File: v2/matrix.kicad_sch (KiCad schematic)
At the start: 136 parts, among them SW10 SW_Push, SW11 SW_Push, SW12 SW_Push, SW13 SW_Push, SW14 SW_Push, SW15 SW_Push, SW16 SW_Push, SW17 SW_Push, SW18 SW_Push, SW19 SW_Push, SW20 SW_Push, SW21 SW_Push, SW22 SW_Push, SW23 SW_Push, SW24 SW_Push, SW25 SW_Push, SW26 SW_Push, SW27 SW_Push, SW28 SW_Push, SW29 SW_Push, SW3 SW_Push, SW30 SW_Push, SW31 SW_Push, SW32 SW_Push, SW33 SW_Push, SW34 SW_Push, SW35 SW_Push, SW36 SW_Push, SW37 SW_Push, SW38 SW_Push, SW39 SW_Push, SW4 SW_Push, SW40 SW_Push, SW41 SW_Push, SW42 SW_Push, SW43 SW_Push, SW44 SW_Push, SW45 SW_Push, SW46 SW_Push, SW47 SW_Push, SW48 SW_Push, SW49 SW_Push, SW5 SW_Push, SW50 SW_Push, SW51 SW_Push, SW52 SW_Push, SW53 SW_Push, SW54 SW_Push, SW55 SW_Push, SW56 SW_Push, SW57 SW_Push, SW58 SW_Push, SW59 SW_Push, SW6 SW_Push, SW60 SW_Push, SW61 SW_Push, SW62 SW_Push, SW63 SW_Push, SW64 SW_Push, SW65 SW_Push, SW66 SW_Push, SW67 SW_Push, SW68 SW_Push, SW69 SW_Push, SW7 SW_Push, SW70 SW_Push, SW8 SW_Push, SW9 SW_Push

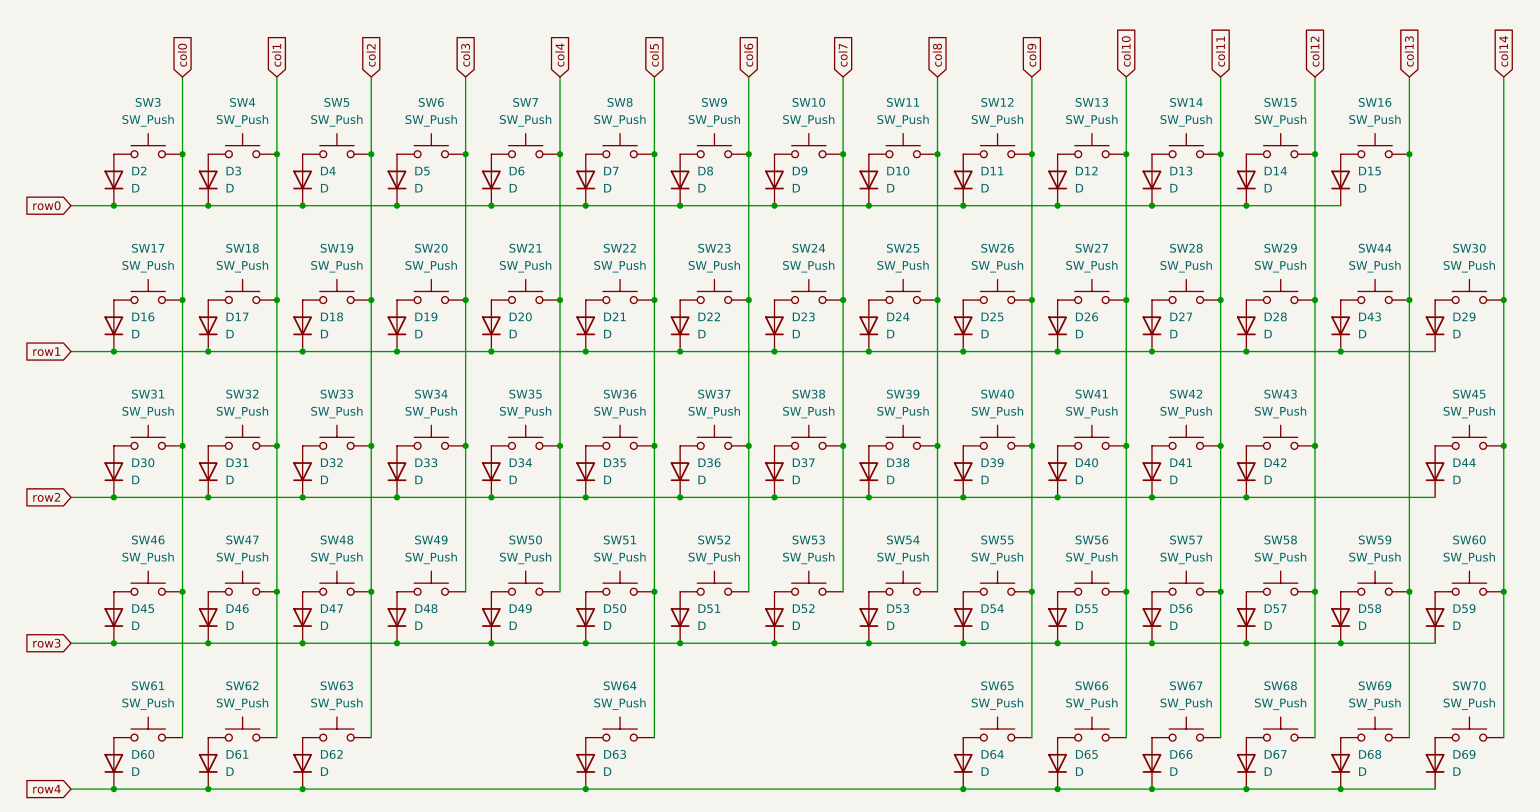
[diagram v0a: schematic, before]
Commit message: Changed switch value for better understanding in PCB view
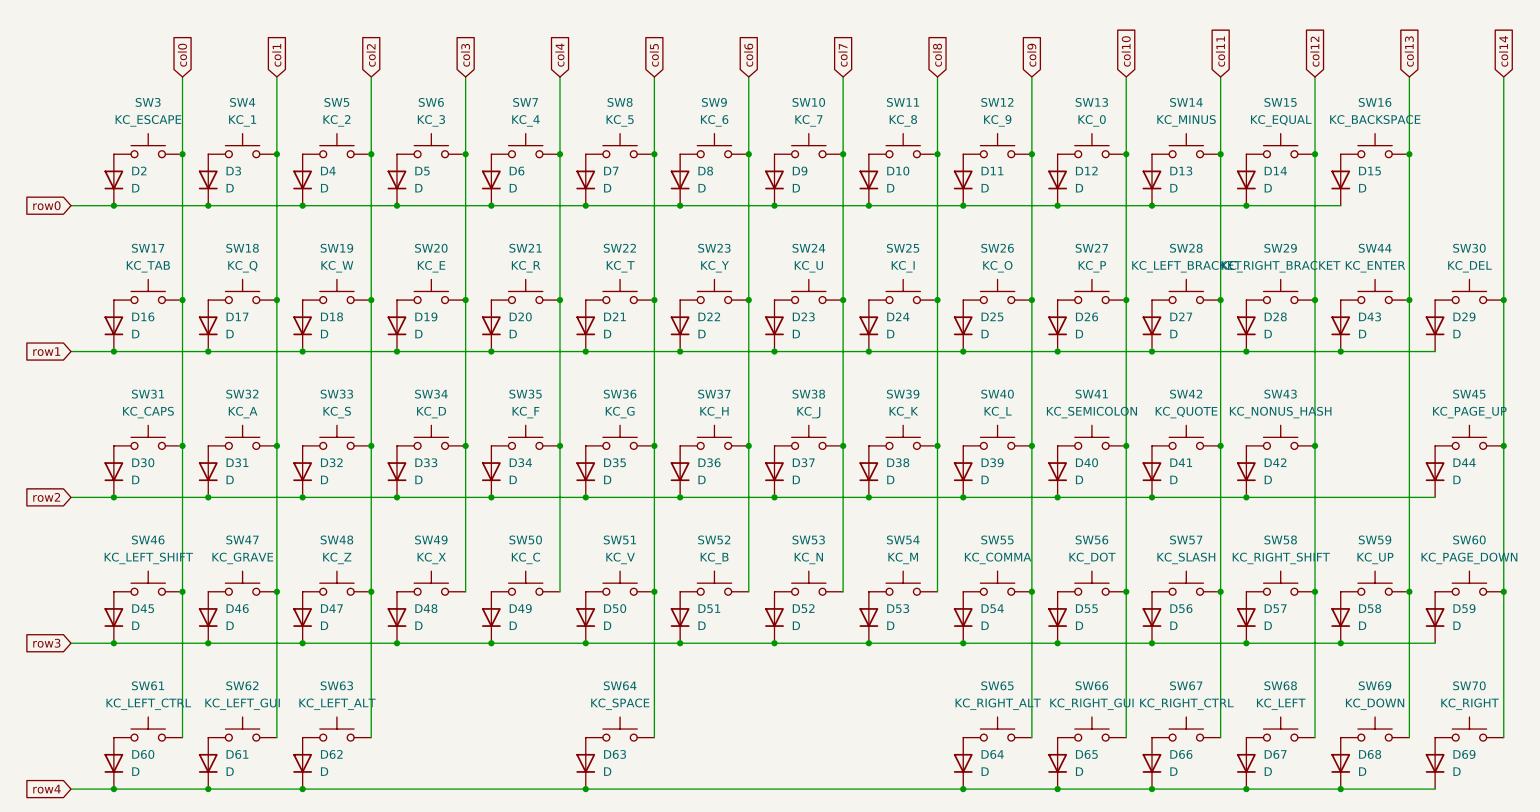
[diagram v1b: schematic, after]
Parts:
- SW10: value SW_Push -> KC_7
- SW11: value SW_Push -> KC_8
- SW12: value SW_Push -> KC_9
- SW13: value SW_Push -> KC_0
- SW14: value SW_Push -> KC_MINUS
- SW15: value SW_Push -> KC_EQUAL
- SW16: value SW_Push -> KC_BACKSPACE
- SW17: value SW_Push -> KC_TAB
- SW18: value SW_Push -> KC_Q
- SW19: value SW_Push -> KC_W
- SW20: value SW_Push -> KC_E
- SW21: value SW_Push -> KC_R
- SW22: value SW_Push -> KC_T
- SW23: value SW_Push -> KC_Y
- SW24: value SW_Push -> KC_U
- SW25: value SW_Push -> KC_I
- SW26: value SW_Push -> KC_O
- SW27: value SW_Push -> KC_P
- SW28: value SW_Push -> KC_LEFT_BRACKET
- SW29: value SW_Push -> KC_RIGHT_BRACKET
- SW3: value SW_Push -> KC_ESCAPE
- SW30: value SW_Push -> KC_DEL
- SW31: value SW_Push -> KC_CAPS
- SW32: value SW_Push -> KC_A
- SW33: value SW_Push -> KC_S
- SW34: value SW_Push -> KC_D
- SW35: value SW_Push -> KC_F
- SW36: value SW_Push -> KC_G
- SW37: value SW_Push -> KC_H
- SW38: value SW_Push -> KC_J
- SW39: value SW_Push -> KC_K
- SW4: value SW_Push -> KC_1
- SW40: value SW_Push -> KC_L
- SW41: value SW_Push -> KC_SEMICOLON
- SW42: value SW_Push -> KC_QUOTE
- SW43: value SW_Push -> KC_NONUS_HASH
- SW44: value SW_Push -> KC_ENTER
- SW45: value SW_Push -> KC_PAGE_UP
- SW46: value SW_Push -> KC_LEFT_SHIFT
- SW47: value SW_Push -> KC_GRAVE
- SW48: value SW_Push -> KC_Z
- SW49: value SW_Push -> KC_X
- SW5: value SW_Push -> KC_2
- SW50: value SW_Push -> KC_C
- SW51: value SW_Push -> KC_V
- SW52: value SW_Push -> KC_B
- SW53: value SW_Push -> KC_N
- SW54: value SW_Push -> KC_M
- SW55: value SW_Push -> KC_COMMA
- SW56: value SW_Push -> KC_DOT
- SW57: value SW_Push -> KC_SLASH
- SW58: value SW_Push -> KC_RIGHT_SHIFT
- SW59: value SW_Push -> KC_UP
- SW6: value SW_Push -> KC_3
- SW60: value SW_Push -> KC_PAGE_DOWN
- SW61: value SW_Push -> KC_LEFT_CTRL
- SW62: value SW_Push -> KC_LEFT_GUI
- SW63: value SW_Push -> KC_LEFT_ALT
- SW64: value SW_Push -> KC_SPACE
- SW65: value SW_Push -> KC_RIGHT_ALT
- SW66: value SW_Push -> KC_RIGHT_GUI
- SW67: value SW_Push -> KC_RIGHT_CTRL
- SW68: value SW_Push -> KC_LEFT
- SW69: value SW_Push -> KC_DOWN
- SW7: value SW_Push -> KC_4
- SW70: value SW_Push -> KC_RIGHT
- SW8: value SW_Push -> KC_5
- SW9: value SW_Push -> KC_6
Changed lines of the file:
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@@
 			)
 		)
-		(property "Value" "SW_Push"
+		(property "Value" "KC_E"
 			(at 121.92 76.2 0)
 			(effects
@@
 			)
 		)
-		(property "Value" "SW_Push"
+		(property "Value" "KC_Q"
 			(at 93.98 76.2 0)
 			(effects
@@
 			)
 		)
-		(property "Value" "SW_Push"
+		(property "Value" "KC_SPACE"
 			(at 149.86 140.97 0)
 			(effects
@@
 			)
 		)
-		(property "Value" "SW_Push"
+		(property "Value" "KC_EQUAL"
 			(at 247.65 54.61 0)
 			(effects
@@
 			)
 		)
-		(property "Value" "SW_Push"
+		(property "Value" "KC_8"
 			(at 191.77 54.61 0)
 			(effects
@@
 			)
 		)
-		(property "Value" "SW_Push"
+		(property "Value" "KC_B"
 			(at 163.83 119.38 0)
 			(effects
@@
 			)
 		)
-		(property "Value" "SW_Push"
+		(property "Value" "KC_T"
 			(at 149.86 76.2 0)
 			(effects
@@
 			)
 		)
-		(property "Value" "SW_Push"
+		(property "Value" "KC_LEFT_ALT"
 			(at 107.95 140.97 0)
 			(effects
@@
 			)
 		)
-		(property "Value" "SW_Push"
+		(property "Value" "KC_RIGHT"
 			(at 275.59 140.97 0)
 			(effects
@@
 			)
 		)
-		(property "Value" "SW_Push"
+		(property "Value" "KC_RIGHT_GUI"
 			(at 219.71 140.97 0)
 			(effects
@@
 			)
 		)
-		(property "Value" "SW_Push"
+		(property "Value" "KC_LEFT_BRACKET"
 			(at 233.68 76.2 0)
 			(effects
@@
 			)
 		)
-		(property "Value" "SW_Push"
+		(property "Value" "KC_LEFT_CTRL"
 			(at 80.01 140.97 0)
 			(effects
@@
 			)
 		)
-		(property "Value" "SW_Push"
+		(property "Value" "KC_4"
 			(at 135.89 54.61 0)
 			(effects
@@
 			)
 		)
-		(property "Value" "SW_Push"
+		(property "Value" "KC_K"
 			(at 191.77 97.79 0)
 			(effects
@@
 			)
 		)
-		(property "Value" "SW_Push"
+		(property "Value" "KC_L"
 			(at 205.74 97.79 0)
 			(effects
@@
 			)
 		)
-		(property "Value" "SW_Push"
+		(property "Value" "KC_LEFT_GUI"
 			(at 93.98 140.97 0)
 			(effects
@@
 			)
 		)
-		(property "Value" "SW_Push"
+		(property "Value" "KC_RIGHT_SHIFT"
 			(at 247.65 119.38 0)
 			(effects
@@
 			)
 		)
-		(property "Value" "SW_Push"
+		(property "Value" "KC_H"
 			(at 163.83 97.79 0)
 			(effects
@@
 			)
 		)
-		(property "Value" "SW_Push"
+		(property "Value" "KC_Y"
 			(at 163.83 76.2 0)
 			(effects
@@
 			)
 		)
-		(property "Value" "SW_Push"
+		(property "Value" "KC_GRAVE"
 			(at 93.98 119.38 0)
 			(effects
@@
 			)
 		)
-		(property "Value" "SW_Push"
+		(property "Value" "KC_NONUS_HASH"
 			(at 247.65 97.79 0)
 			(effects
@@
 			)
 		)
-		(property "Value" "SW_Push"
+		(property "Value" "KC_O"
 			(at 205.74 76.2 0)
 			(effects
@@
 			)
 		)
-		(property "Value" "SW_Push"
+		(property "Value" "KC_QUOTE"
 			(at 233.68 97.79 0)
 			(effects
@@
 			)
 		)
-		(property "Value" "SW_Push"
+		(property "Value" "KC_1"
 			(at 93.98 54.61 0)
 			(effects
@@
 			)
 		)
-		(property "Value" "SW_Push"
+		(property "Value" "KC_COMMA"
 			(at 205.74 119.38 0)
 			(effects
@@
 			)
 		)
-		(property "Value" "SW_Push"
+		(property "Value" "KC_TAB"
 			(at 80.01 76.2 0)
 			(effects
@@
 			)
 		)
-		(property "Value" "SW_Push"
+		(property "Value" "KC_BACKSPACE"
 			(at 261.62 54.61 0)
 			(effects
@@
 			)
 		)
-		(property "Value" "SW_Push"
+		(property "Value" "KC_LEFT"
 			(at 247.65 140.97 0)
 			(effects
@@
 			)
 		)
-		(property "Value" "SW_Push"
+		(property "Value" "KC_C"
 			(at 135.89 119.38 0)
 			(effects
@@
 			)
 		)
-		(property "Value" "SW_Push"
+		(property "Value" "KC_9"
 			(at 205.74 54.61 0)
 			(effects
@@
 			)
 		)
-		(property "Value" "SW_Push"
+		(property "Value" "KC_3"
 			(at 121.92 54.61 0)
 			(effects
@@
 			)
 		)
-		(property "Value" "SW_Push"
+		(property "Value" "KC_SEMICOLON"
 			(at 219.71 97.79 0)
 			(effects
@@
 			)
 		)
-		(property "Value" "SW_Push"
+		(property "Value" "KC_DEL"
 			(at 275.59 76.2 0)
 			(effects
@@
 			)
 		)
-		(property "Value" "SW_Push"
+		(property "Value" "KC_SLASH"
 			(at 233.68 119.38 0)
 			(effects
@@
 			)
 		)
-		(property "Value" "SW_Push"
+		(property "Value" "KC_RIGHT_ALT"
 			(at 205.74 140.97 0)
 			(effects
@@
 			)
 		)
-		(property "Value" "SW_Push"
+		(property "Value" "KC_G"
 			(at 149.86 97.79 0)
 			(effects
@@
 			)
 		)
-		(property "Value" "SW_Push"
+		(property "Value" "KC_DOWN"
 			(at 261.62 140.97 0)
 			(effects
@@
 			)
 		)
-		(property "Value" "SW_Push"
+		(property "Value" "KC_P"
 			(at 219.71 76.2 0)
 			(effects
@@
 			)
 		)
-		(property "Value" "SW_Push"
+		(property "Value" "KC_A"
 			(at 93.98 97.79 0)
 			(effects
@@
 			)
 		)
-		(property "Value" "SW_Push"
+		(property "Value" "KC_W"
 			(at 107.95 76.2 0)
 			(effects
@@
 			)
 		)
-		(property "Value" "SW_Push"
+		(property "Value" "KC_S"
 			(at 107.95 97.79 0)
 			(effects
@@
 			)
 		)
-		(property "Value" "SW_Push"
+		(property "Value" "KC_ESCAPE"
 			(at 80.01 54.61 0)
 			(effects
@@
 			)
 		)
-		(property "Value" "SW_Push"
+		(property "Value" "KC_RIGHT_BRACKET"
 			(at 247.65 76.2 0)
 			(effects
@@
 			)
 		)
-		(property "Value" "SW_Push"
+		(property "Value" "KC_I"
 			(at 191.77 76.2 0)
 			(effects
@@
 			)
 		)
-		(property "Value" "SW_Push"
+		(property "Value" "KC_RIGHT_CTRL"
 			(at 233.68 140.97 0)
 			(effects
@@
 			)
 		)
-		(property "Value" "SW_Push"
+		(property "Value" "KC_U"
 			(at 177.8 76.2 0)
 			(effects
@@
 			)
 		)
-		(property "Value" "SW_Push"
+		(property "Value" "KC_6"
 			(at 163.83 54.61 0)
 			(effects
@@
 			)
 		)
-		(property "Value" "SW_Push"
+		(property "Value" "KC_PAGE_UP"
 			(at 275.59 97.79 0)
 			(effects
@@
 			)
 		)
-		(property "Value" "SW_Push"
+		(property "Value" "KC_5"
 			(at 149.86 54.61 0)
 			(effects
@@
 			)
 		)
-		(property "Value" "SW_Push"
+		(property "Value" "KC_2"
 			(at 107.95 54.61 0)
 			(effects
@@
 			)
 		)
-		(property "Value" "SW_Push"
+		(property "Value" "KC_Z"
 			(at 107.95 119.38 0)
 			(effects
@@
 			)
 		)
-		(property "Value" "SW_Push"
+		(property "Value" "KC_ENTER"
 			(at 261.62 76.2 0)
 			(effects
@@
 			)
 		)
-		(property "Value" "SW_Push"
+		(property "Value" "KC_DOT"
 			(at 219.71 119.38 0)
 			(effects
@@
 			)
 		)
-		(property "Value" "SW_Push"
+		(property "Value" "KC_J"
 			(at 177.8 97.79 0)
 			(effects
@@
 			)
 		)
-		(property "Value" "SW_Push"
+		(property "Value" "KC_PAGE_DOWN"
 			(at 275.59 119.38 0)
 			(effects
@@
 			)
 		)
-		(property "Value" "SW_Push"
+		(property "Value" "KC_7"
 			(at 177.8 54.61 0)
 			(effects
@@
 			)
 		)
-		(property "Value" "SW_Push"
+		(property "Value" "KC_LEFT_SHIFT"
 			(at 80.01 119.38 0)
 			(effects
@@
 			)
 		)
-		(property "Value" "SW_Push"
+		(property "Value" "KC_0"
 			(at 219.71 54.61 0)
 			(effects
@@
 			)
 		)
-		(property "Value" "SW_Push"
+		(property "Value" "KC_X"
 			(at 121.92 119.38 0)
 			(effects
@@
 			)
 		)
-		(property "Value" "SW_Push"
+		(property "Value" "KC_CAPS"
 			(at 80.01 97.79 0)
 			(effects
@@
 			)
 		)
-		(property "Value" "SW_Push"
+		(property "Value" "KC_UP"
 			(at 261.62 119.38 0)
 			(effects
@@
 			)
 		)
-		(property "Value" "SW_Push"
+		(property "Value" "KC_N"
 			(at 177.8 119.38 0)
 			(effects
@@
 			)
 		)
-		(property "Value" "SW_Push"
+		(property "Value" "KC_R"
 			(at 135.89 76.2 0)
 			(effects
@@
 			)
 		)
-		(property "Value" "SW_Push"
+		(property "Value" "KC_D"
 			(at 121.92 97.79 0)
 			(effects
@@
 			)
 		)
-		(property "Value" "SW_Push"
+		(property "Value" "KC_M"
 			(at 191.77 119.38 0)
 			(effects
@@
 			)
 		)
-		(property "Value" "SW_Push"
+		(property "Value" "KC_MINUS"
 			(at 233.68 54.61 0)
 			(effects
@@
 			)
 		)
-		(property "Value" "SW_Push"
+		(property "Value" "KC_V"
 			(at 149.86 119.38 0)
 			(effects
@@
 			)
 		)
-		(property "Value" "SW_Push"
+		(property "Value" "KC_F"
 			(at 135.89 97.79 0)
 			(effects

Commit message: Changed switch footprint to MX footprint
Realised I didn't want Alp switch so changed to more classic MX switch.
Need a full redone of the routing :'(
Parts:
- SW10, SW11, SW12, SW13, SW14, SW15, SW18, SW19, SW20, SW21, SW22, SW23, SW24, SW25, SW26, SW27, SW28, SW29, SW3, SW30, SW32, SW33, SW34, SW35, SW36, SW37, SW38, SW39, SW4, SW40, SW41, SW42, SW43, SW45, SW47, SW48, SW49, SW5, SW50, SW51, SW52, SW53, SW54, SW55, SW56, SW57, SW59, SW6, SW60, SW65, SW66, SW67, SW68, SW69, SW7, SW70, SW8, SW9: footprint Alps_Only:ALPS-1U -> Button_Switch_Keyboard:SW_Cherry_MX_1.00u_PCB
- SW16: footprint Alps_Only:ALPS-2U -> Button_Switch_Keyboard:SW_Cherry_MX_2.00u_PCB
- SW17: footprint Alps_Only:ALPS-1.5U -> Button_Switch_Keyboard:SW_Cherry_MX_1.50u_PCB
- SW31, SW58: footprint Alps_Only:ALPS-1.75U -> Button_Switch_Keyboard:SW_Cherry_MX_1.75u_PCB
- SW44: footprint Alps_Only:ALPS-ISO -> Button_Switch_Keyboard:SW_Cherry_MX_ISOEnter_PCB
- SW46, SW61, SW62, SW63: footprint Alps_Only:ALPS-1.25U -> Button_Switch_Keyboard:SW_Cherry_MX_1.25u_PCB
- SW64: footprint Alps_Only:ALPS-6.25U -> Button_Switch_Keyboard:SW_Cherry_MX_6.25u_PCB
